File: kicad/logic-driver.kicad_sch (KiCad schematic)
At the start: 27 parts, among them J1 TIMEPULSE, J2 TIMEPULSE2, J3 LCD signal, J4 LCD GND, J5 LCD bias, J6 LCD bias, U3 4011, U4 4070, U5 4013, U6 TL074

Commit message: Rewires the D-flipflop divider to have signal C in phase with TIMEPULSE
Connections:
- net GND: no longer U5.4 (R)
- net at J2.1 (Pin_1), U3.6, U5.3 (C): no longer U3.2
- net at J1.1 (Pin_1), U3.1: now also U3.2, U5.4 (R)
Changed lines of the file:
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@@
   (junction (at 121.92 104.14) (diameter 0) (color 0 0 0 0)
   )
+  (junction (at 63.5 50.8) (diameter 0) (color 0 0 0 0)
+  )
   (junction (at 152.4 58.42) (diameter 0) (color 0 0 0 0)
   )
-  (junction (at 60.96 50.8) (diameter 0) (color 0 0 0 0)
-  )
   (junction (at 215.9 64.77) (diameter 0) (color 0 0 0 0)
   )
@@
   (junction (at 130.81 48.26) (diameter 0) (color 0 0 0 0)
   )
-  (junction (at 60.96 48.26) (diameter 0) (color 0 0 0 0)
-  )
   (junction (at 186.69 76.2) (diameter 0) (color 0 0 0 0)
   )
@@
   (junction (at 132.08 78.74) (diameter 0) (color 0 0 0 0)
   )
+  (junction (at 60.96 45.72) (diameter 0) (color 0 0 0 0)
+  )
+  (junction (at 66.04 45.72) (diameter 0) (color 0 0 0 0)
+  )
   (junction (at 121.92 78.74) (diameter 0) (color 0 0 0 0)
   )
@@
     (stroke (width 0) (type default))
   )
+  (wire (pts (xy 60.96 85.09) (xy 76.2 85.09))
+    (stroke (width 0) (type default))
+  )
   (wire (pts (xy 130.81 58.42) (xy 130.81 59.69))
     (stroke (width 0) (type default))
@@
     (stroke (width 0) (type default))
   )
-  (wire (pts (xy 60.96 73.66) (xy 68.58 73.66))
+  (wire (pts (xy 66.04 48.26) (xy 68.58 48.26))
     (stroke (width 0) (type default))
   )
@@
     (stroke (width 0) (type default))
   )
+  (wire (pts (xy 68.58 43.18) (xy 66.04 43.18))
+    (stroke (width 0) (type default))
+  )
   (wire (pts (xy 177.8 40.64) (xy 177.8 50.8))
     (stroke (width 0) (type default))
@@
     (stroke (width 0) (type default))
   )
+  (wire (pts (xy 68.58 73.66) (xy 63.5 73.66))
+    (stroke (width 0) (type default))
+  )
+  (wire (pts (xy 63.5 50.8) (xy 88.9 50.8))
+    (stroke (width 0) (type default))
+  )
   (wire (pts (xy 215.9 64.77) (xy 218.44 64.77))
     (stroke (width 0) (type default))
   )
-  (wire (pts (xy 59.69 43.18) (xy 68.58 43.18))
-    (stroke (width 0) (type default))
-  )
-  (wire (pts (xy 60.96 50.8) (xy 88.9 50.8))
-    (stroke (width 0) (type default))
-  )
   (wire (pts (xy 83.82 76.2) (xy 87.63 76.2))
     (stroke (width 0) (type default))
@@
     (stroke (width 0) (type default))
   )
+  (wire (pts (xy 59.69 50.8) (xy 63.5 50.8))
+    (stroke (width 0) (type default))
+  )
   (wire (pts (xy 121.92 78.74) (xy 132.08 78.74))
     (stroke (width 0) (type default))
@@
     (stroke (width 0) (type default))
   )
-  (wire (pts (xy 60.96 48.26) (xy 68.58 48.26))
-    (stroke (width 0) (type default))
-  )
-  (wire (pts (xy 60.96 48.26) (xy 60.96 50.8))
+  (wire (pts (xy 63.5 50.8) (xy 63.5 73.66))
     (stroke (width 0) (type default))
   )
@@
     (stroke (width 0) (type default))
   )
+  (wire (pts (xy 60.96 45.72) (xy 66.04 45.72))
+    (stroke (width 0) (type default))
+  )
   (wire (pts (xy 144.78 58.42) (xy 152.4 58.42))
     (stroke (width 0) (type default))
@@
     (stroke (width 0) (type default))
   )
-  (wire (pts (xy 60.96 50.8) (xy 60.96 73.66))
-    (stroke (width 0) (type default))
-  )
   (wire (pts (xy 215.9 53.34) (xy 218.44 53.34))
     (stroke (width 0) (type default))
@@
     (stroke (width 0) (type default))
   )
-  (wire (pts (xy 59.69 48.26) (xy 60.96 48.26))
-    (stroke (width 0) (type default))
-  )
   (wire (pts (xy 121.92 101.6) (xy 121.92 104.14))
     (stroke (width 0) (type default))
@@
     (stroke (width 0) (type default))
   )
+  (wire (pts (xy 60.96 45.72) (xy 60.96 85.09))
+    (stroke (width 0) (type default))
+  )
   (wire (pts (xy 181.61 76.2) (xy 186.69 76.2))
     (stroke (width 0) (type default))
@@
     (stroke (width 0) (type default))
   )
+  (wire (pts (xy 66.04 43.18) (xy 66.04 45.72))
+    (stroke (width 0) (type default))
+  )
   (wire (pts (xy 83.82 45.72) (xy 88.9 45.72))
     (stroke (width 0) (type default))
@@
     (stroke (width 0) (type default))
   )
+  (wire (pts (xy 66.04 45.72) (xy 66.04 48.26))
+    (stroke (width 0) (type default))
+  )
   (wire (pts (xy 205.74 53.34) (xy 205.74 76.2))
     (stroke (width 0) (type default))
@@
     (stroke (width 0) (type default))
   )
+  (wire (pts (xy 76.2 81.28) (xy 76.2 85.09))
+    (stroke (width 0) (type default))
+  )
   (wire (pts (xy 92.71 71.12) (xy 111.76 71.12))
+    (stroke (width 0) (type default))
+  )
+  (wire (pts (xy 59.69 45.72) (xy 60.96 45.72))
     (stroke (width 0) (type default))
   )
@@
     )
   )
-  (symbol (lib_id "Connector_Generic:Conn_01x01") (at 223.52 53.34 0) (unit 1)
+  (symbol (lib_name "Conn_01x01_3") (lib_id "Connector_Generic:Conn_01x01") (at 223.52 53.34 0) (unit 1)
     (in_bom yes) (on_board yes) (dnp no)
     (property "Reference" "J3" (at 226.06 52.07 0)
@@
     )
   )
-  (symbol (lib_id "Connector_Generic:Conn_01x01") (at 223.52 76.2 0) (unit 1)
+  (symbol (lib_name "Conn_01x01_5") (lib_id "Connector_Generic:Conn_01x01") (at 223.52 76.2 0) (unit 1)
     (in_bom yes) (on_board yes) (dnp no)
     (property "Reference" "J6" (at 226.06 74.93 0)
@@
     )
   )
-  (symbol (lib_id "Connector_Generic:Conn_01x01") (at 54.61 43.18 0) (mirror y) (unit 1)
-    (in_bom yes) (on_board yes) (dnp no) (fields_autoplaced)
-    (property "Reference" "J1" (at 52.07 41.91 0)
-      (effects (font (size 1.27 1.27)) (justify left))
-    )
-    (property "Value" "TIMEPULSE" (at 52.07 44.45 0)
-      (effects (font (size 1.27 1.27)) (justify left))
-    )
-    (property "Footprint" "" (at 54.61 43.18 0)
-      (effects (font (size 1.27 1.27)) hide)
-    )
-    (property "Datasheet" "~" (at 54.61 43.18 0)
+  (symbol (lib_name "Conn_01x01_1") (lib_id "Connector_Generic:Conn_01x01") (at 54.61 45.72 0) (mirror y) (unit 1)
+    (in_bom yes) (on_board yes) (dnp no) (fields_autoplaced)
+    (property "Reference" "J1" (at 52.07 44.45 0)
+      (effects (font (size 1.27 1.27)) (justify left))
+    )
+    (property "Value" "TIMEPULSE" (at 52.07 46.99 0)
+      (effects (font (size 1.27 1.27)) (justify left))
+    )
+    (property "Footprint" "" (at 54.61 45.72 0)
+      (effects (font (size 1.27 1.27)) hide)
+    )
+    (property "Datasheet" "~" (at 54.61 45.72 0)
       (effects (font (size 1.27 1.27)) hide)
     )
@@
     )
   )
-  (symbol (lib_id "Connector_Generic:Conn_01x01") (at 54.61 48.26 0) (mirror y) (unit 1)
-    (in_bom yes) (on_board yes) (dnp no) (fields_autoplaced)
-    (property "Reference" "J2" (at 52.07 46.99 0)
-      (effects (font (size 1.27 1.27)) (justify left))
-    )
-    (property "Value" "TIMEPULSE2" (at 52.07 49.53 0)
-      (effects (font (size 1.27 1.27)) (justify left))
-    )
-    (property "Footprint" "" (at 54.61 48.26 0)
-      (effects (font (size 1.27 1.27)) hide)
-    )
-    (property "Datasheet" "~" (at 54.61 48.26 0)
+  (symbol (lib_name "Conn_01x01_2") (lib_id "Connector_Generic:Conn_01x01") (at 54.61 50.8 0) (mirror y) (unit 1)
+    (in_bom yes) (on_board yes) (dnp no) (fields_autoplaced)
+    (property "Reference" "J2" (at 52.07 49.53 0)
+      (effects (font (size 1.27 1.27)) (justify left))
+    )
+    (property "Value" "TIMEPULSE2" (at 52.07 52.07 0)
+      (effects (font (size 1.27 1.27)) (justify left))
+    )
+    (property "Footprint" "" (at 54.61 50.8 0)
+      (effects (font (size 1.27 1.27)) hide)
+    )
+    (property "Datasheet" "~" (at 54.61 50.8 0)
       (effects (font (size 1.27 1.27)) hide)
     )
@@
         (path "/05cf2ea0-cbb3-483a-be66-aa338cfbdd07"
           (reference "J2") (unit 1)
-        )
-      )
-    )
-  )
-  (symbol (lib_id "power:GND") (at 76.2 81.28 0) (unit 1)
-    (in_bom yes) (on_board yes) (dnp no)
-    (property "Reference" "#PWR05" (at 76.2 87.63 0)
-      (effects (font (size 1.27 1.27)) hide)
-    )
-    (property "Value" "GND" (at 72.39 83.82 0)
-      (effects (font (size 1.27 1.27)))
-    )
-    (property "Footprint" "" (at 76.2 81.28 0)
-      (effects (font (size 1.27 1.27)) hide)
-    )
-    (property "Datasheet" "" (at 76.2 81.28 0)
-      (effects (font (size 1.27 1.27)) hide)
-    )
-    (pin "1")
-    (instances
-      (project "logic-driver"
-        (path "/05cf2ea0-cbb3-483a-be66-aa338cfbdd07"
-          (reference "#PWR05") (unit 1)
         )
       )
@@
     )
   )
-  (symbol (lib_id "Connector_Generic:Conn_01x01") (at 223.52 64.77 0) (unit 1)
+  (symbol (lib_name "Conn_01x01_4") (lib_id "Connector_Generic:Conn_01x01") (at 223.52 64.77 0) (unit 1)
     (in_bom yes) (on_board yes) (dnp no)
     (property "Reference" "J5" (at 226.06 63.5 0)

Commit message: Updates the electronic schema
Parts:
- removed R11: 10, symbol Device:R
- removed R12: 1M, symbol Device:R
- removed R3: 100k, symbol Device:R
- removed RV1: 10k, symbol Device:R_Potentiometer
- removed U4: 4070, symbol 4xxx:4070
- removed U5: 4013, symbol 4xxx:4013
- removed U6: TL074, symbol Amplifier_Operational:TL074
- added C2: 100 pF, symbol Device:C
- added D1: Photo, symbol Device:D_Photo_Filled
- added D2: LED, symbol Device:LED_Filled
- added J7: Photo signal, symbol Connector_Generic:Conn_01x01
- added R3: 47k, symbol Device:R_Trim
- added TP4: Signal G, symbol Connector:TestPoint
- added TP5: Signal H, symbol Connector:TestPoint
- added TP6: Signal I, symbol Connector:TestPoint
- added U1: 4011, symbol 4xxx:4011
- added U2: 4013, symbol 4xxx:4013
- added U4: TL074, symbol Amplifier_Operational:TL074
- C1: value 1uF -> 1 uF
- J3: value LCD signal -> LCD drive
- J4: value LCD GND -> LCD bias
- J5: value LCD bias -> LCD GND
- J6: value LCD bias -> Photo GND
- R1: value 10k -> 100k
- R10, R8: value 100k -> 1M
- R2: value 10k -> 82k
- R7: value 100k -> 270
- R9: value 10k -> 330
- TP3: value Signal E -> Signal F
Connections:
- net GND: now also C1.2, J5.1 (Pin_1), J6.1 (Pin_1), D1.2 (A), D2.1 (K), U1.7 (VSS), U2.6 (S), U2.7 (VSS), U4.10 (+), U4.3 (+), U4.5 (+); no longer J4.1 (Pin_1), R8.2
- net at U3.8, U3.9: now also U1.11; no longer U3.4
- net at TP1.1: now also U3.1, U1.10, U1.12
- net at J2.1 (Pin_1): now also U1.6, U2.3 (C); no longer U3.6
- net at U3.3, U3.5: now also U3.6
- net at R1.2, R2.1: now also U4.2 (-)
- net at R2.2: now also R3.1
- net at TP3.1: now also R1.1, U3.4; no longer R4.1
- net at R4.2: now also R5.2, R6.1, U4.6 (-); no longer R7.1
- net at R8.1: now also J3.1 (Pin_1), R7.2, TP5.1
- net at R9.2: now also D2.2 (A); no longer R10.2
- net +5V: now reaches R9.1
- net +5V: now also U3.14 (VDD), U1.14 (VDD), U2.14 (VDD)
- net at C1.1: now also J4.1 (Pin_1), R8.2; no longer J5.1 (Pin_1)
- net +15V: no longer names the net of R5.1
- net +15V: now also U4.13 (-), U4.14; no longer U3.14 (VDD)
- net -15V: no longer names the net of R6.2
- net -15V: now also R7.1, U4.7
- new net: U1.13, U2.2 (~{Q}), U2.5 (D)
- new net: TP4.1, U3.10, U4.12 (+)
- new net: J1.1 (Pin_1), U1.1, U1.2, U2.4 (R)
- new net: C2.2, J7.1 (Pin_1), R10.2, TP6.1, U4.8
- new net: R3.2, R4.1, U4.1
- new net: U1.4, U1.8, U1.9
- new net: U1.3, U1.5
- new net: C2.1, D1.1 (K), R10.1, U4.9 (-)
- new net: TP2.1, U2.1 (Q), U3.2
- new net +12V: U4.4 (V+)
- new net -12V: U4.11 (V-)

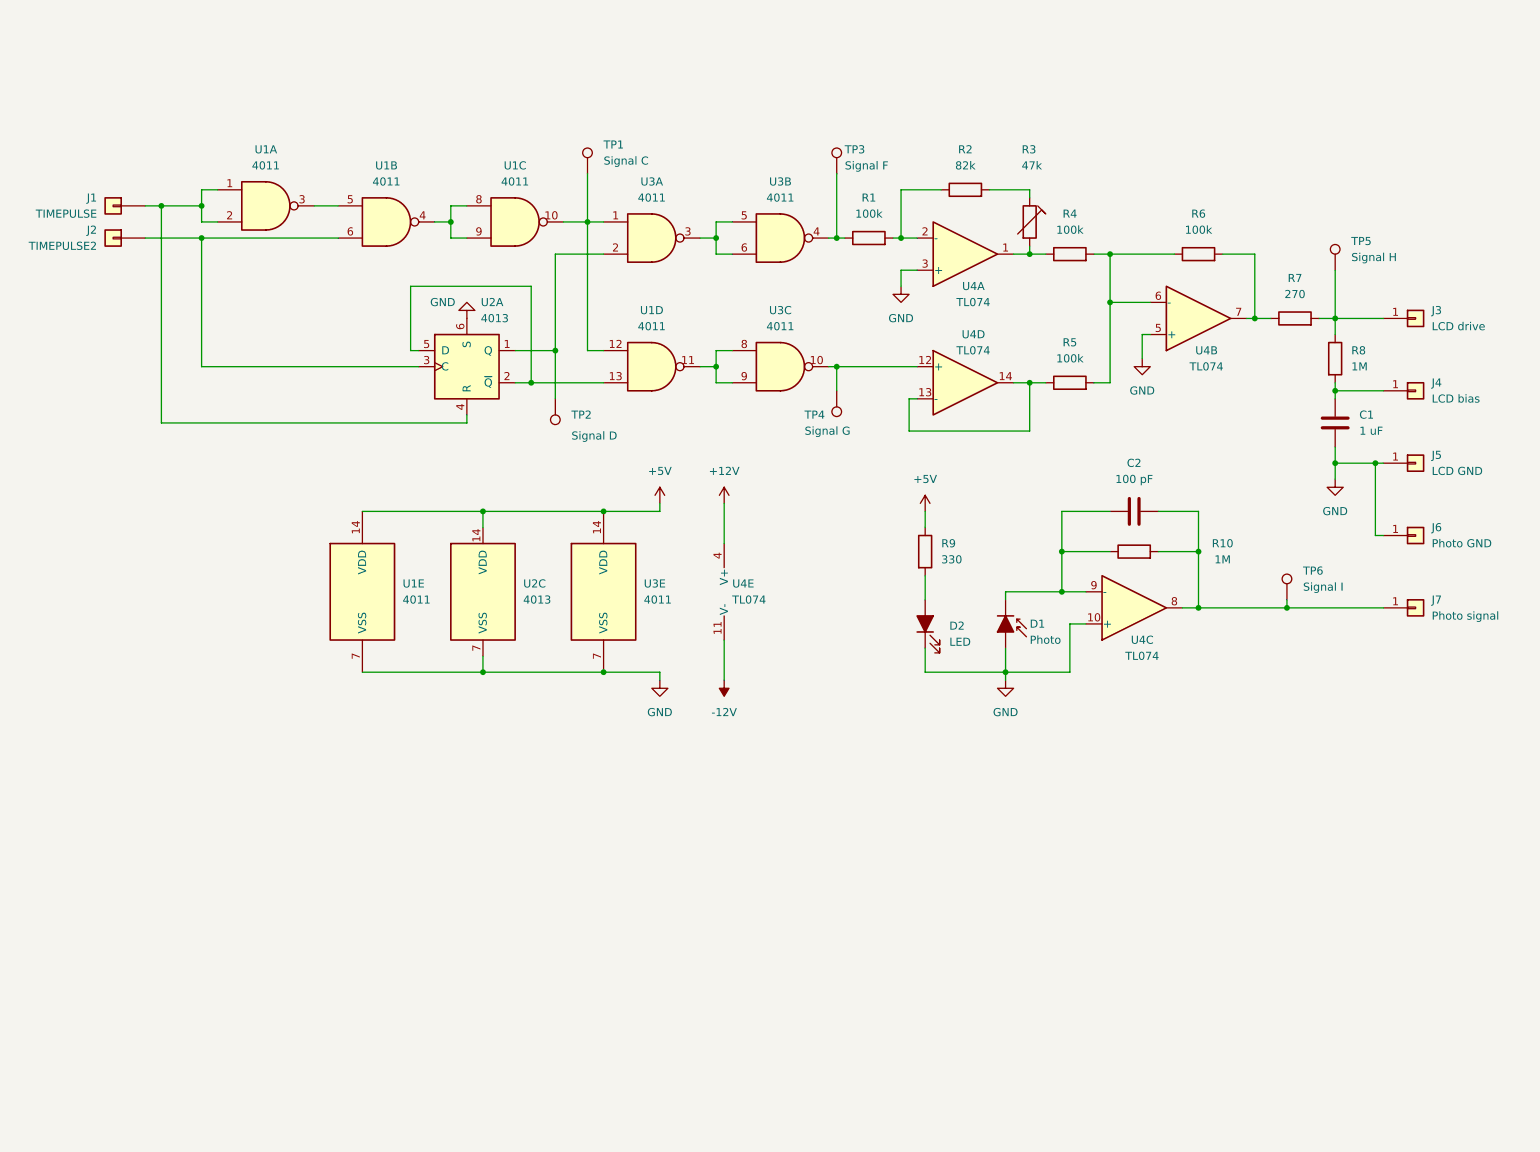
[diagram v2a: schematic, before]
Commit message: Update schema regarding voltage follower
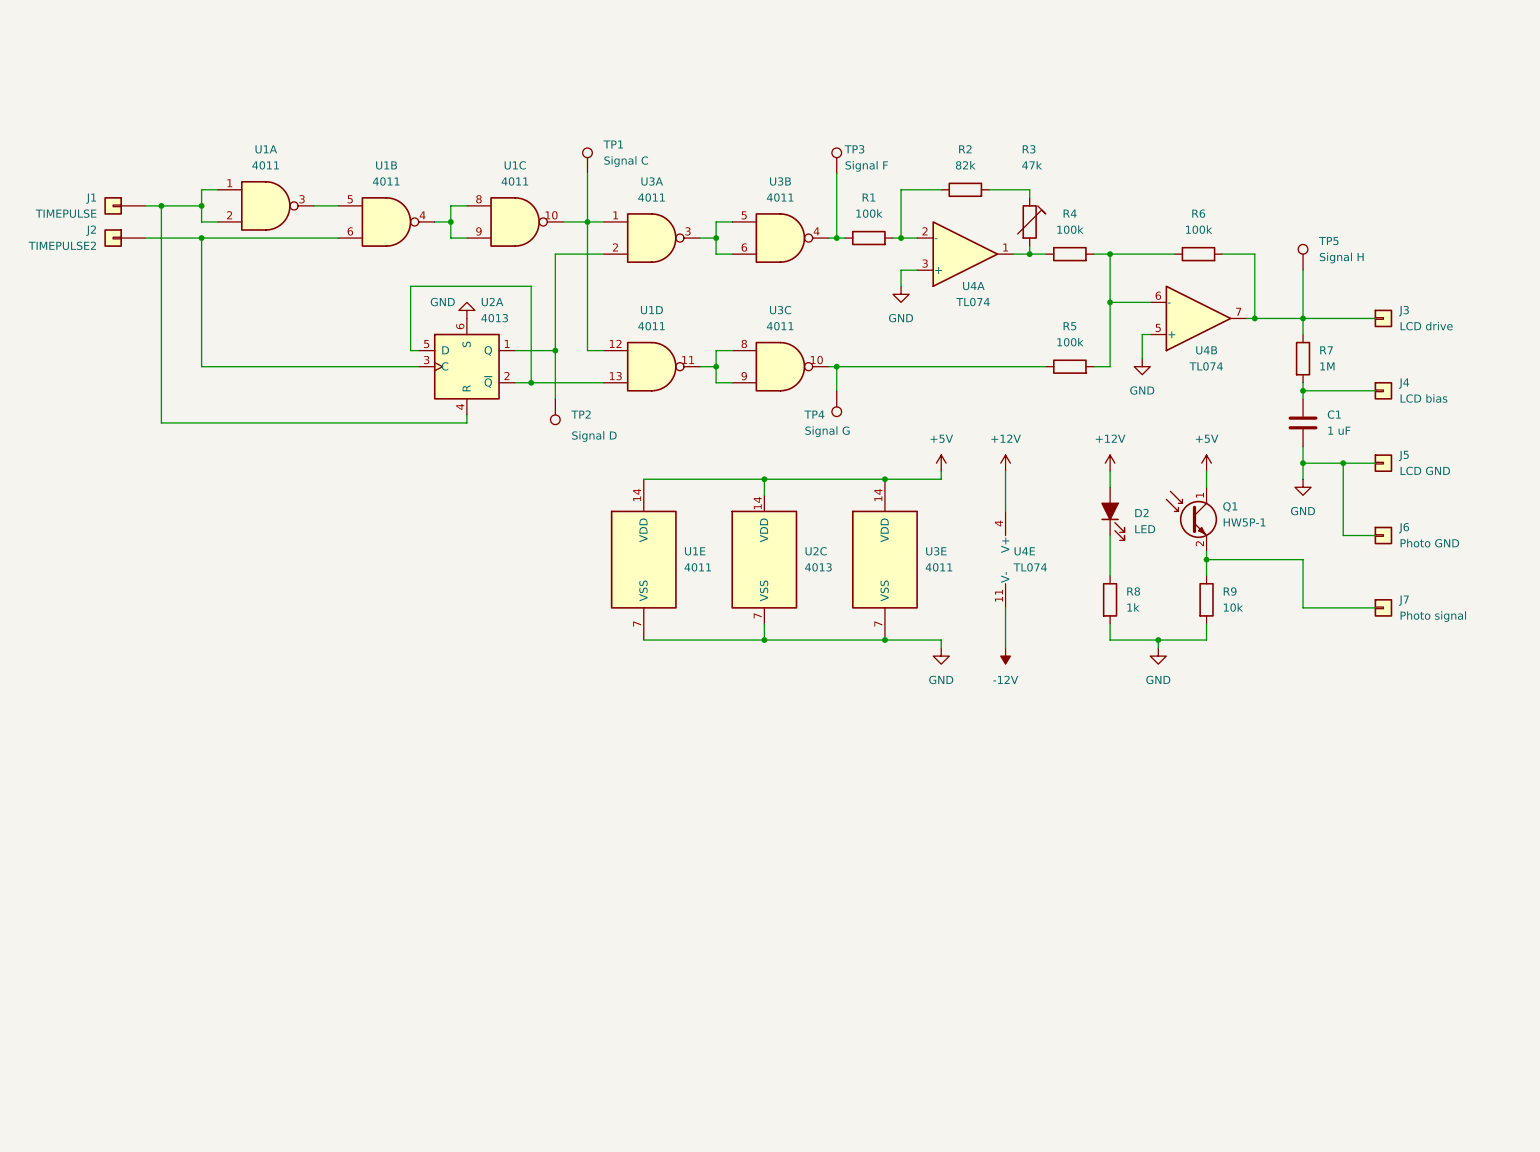
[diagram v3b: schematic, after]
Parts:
- removed C2: 100 pF, symbol Device:C
- removed D1: Photo, symbol Device:D_Photo_Filled
- removed R10: 1M, symbol Device:R
- removed R7: 270, symbol Device:R
- removed TP6: Signal I, symbol Connector:TestPoint
- removed unit 3 of U4
- removed unit 4 of U4
- added Q1: HW5P-1, LED_THT:LED_D5.0mm_Clear, symbol Sensor_Optical:BPW40
- added R9: 10k, symbol Device:R
- R8: renamed from R9; value 330 -> 1k
- renumbered R8 to R7
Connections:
- net +12V: now also D2.2 (A)
- net +5V: now also Q1.1 (C); no longer R8.1
- net GND: now also R8.2, R9.2; no longer D2.1 (K), J5.1 (Pin_1), J6.1 (Pin_1)
- net at R5.1: now also TP4.1, U3.10
- net at R6.2, U4.7: now also R7.1, TP5.1
- net at C1.1, R7.2: no longer J4.1 (Pin_1)
- new net: D2.1 (K), R8.1
- new net: Q1.2 (E), R9.1
- now unconnected: J3.1 (Pin_1)
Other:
- moved on the sheet: C1, D2, R5, R7, R8, TP5, U1E, U2C, U3E, U4E
